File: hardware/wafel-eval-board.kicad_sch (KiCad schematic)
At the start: 50 parts, among them J101 CAN PORT, J102 SW, Q101 AO3422, U101 LM5163DDA

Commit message: reduced BOM
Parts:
- F103: footprint wafel-eval-board:Fuse_SMD-3P_5.4x3.2mm -> wafel-eval-board:Fuse_ITV5432
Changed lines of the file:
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@@
 			)
 		)
-		(property "Footprint" "wafel-eval-board:Fuse_SMD-3P_5.4x3.2mm"
+		(property "Footprint" "wafel-eval-board:Fuse_ITV5432"
 			(at 215.9 134.62 0)
 			(hide yes)

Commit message: increased size two times
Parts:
- JP101: footprint Jumper:SolderJumper-3_P2.0mm_Open_TrianglePad1.0x1.5mm -> Jumper:SolderJumper-3_P1.3mm_Open_Pad1.0x1.5mm
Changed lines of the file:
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@@
 			)
 		)
-		(property "Footprint" "Jumper:SolderJumper-3_P2.0mm_Open_TrianglePad1.0x1.5mm"
+		(property "Footprint" "Jumper:SolderJumper-3_P1.3mm_Open_Pad1.0x1.5mm"
 			(at 242.57 125.73 0)
 			(hide yes)

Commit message: ADD ZONES
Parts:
- added H117: BAT+, MountingHole:MountingHole_3.2mm_M3_Pad, symbol Mechanical:MountingHole_Pad
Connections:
- net CELL10: no longer F102.1, F103.1
- new net: F102.1, F103.1, H117.1
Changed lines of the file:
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@@
 		)
 	)
-	(label "CELL10"
-		(at 204.47 142.24 180)
-		(effects
-			(font
-				(size 1.27 1.27)
-			)
-			(justify right bottom)
-		)
-	)
 	(label "FUSE"
 		(at 139.7 77.47 180)
@@
 					(unit 1)
 				)
+			)
+		)
+	)
+	(symbol
+		(lib_id "Mechanical:MountingHole_Pad")
+		(at 201.93 142.24 90)
+		(mirror x)
+		(unit 1)
+		(body_style 1)
+		(exclude_from_sim no)
+		(in_bom no)
+		(on_board yes)
+		(in_pos_files yes)
+		(dnp no)
+		(property "Reference" "H117"
+			(at 193.04 140.97 90)
+			(show_name no)
+			(do_not_autoplace no)
+			(effects
+				(font
+					(size 1.27 1.27)
+				)
+				(justify right)
+			)
+		)
+		(property "Value" "BAT+"
+			(at 193.04 143.51 90)
+			(show_name no)
+			(do_not_autoplace no)
+			(effects
+				(font
+					(size 1.27 1.27)
+				)
+				(justify right)
+			)
+		)
+		(property "Footprint" "MountingHole:MountingHole_3.2mm_M3_Pad"
+			(at 201.93 142.24 0)
+			(hide yes)
+			(show_name no)
+			(do_not_autoplace no)
+			(effects
+				(font
+					(size 1.27 1.27)
+				)
+			)
+		)
+		(property "Datasheet" ""
+			(at 201.93 142.24 0)
+			(hide yes)
+			(show_name no)
+			(do_not_autoplace no)
+			(effects
+				(font
+					(size 1.27 1.27)
+				)
+			)
+		)
+		(property "Description" "Mounting Hole with connection"
+			(at 201.93 142.24 0)
+			(hide yes)
+			(show_name no)
+			(do_not_autoplace no)
+			(effects
+				(font
+					(size 1.27 1.27)
+				)
+			)
+		)
+		(pin "1"
+		)
+		(instances
+			(project "wafel-eval-board"
+				(path "/3e668e3e-3e16-4665-a807-4735962c41d3"
+					(reference "H117")
+					(unit 1)
+				)

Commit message: Actualize resistors size
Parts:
- added R112: 0, Resistor_SMD:R_0603_1608Metric, symbol Device:R_Small
- D102: footprint LED_THT:LED_D3.0mm -> LED_SMD:LED_0201_0603Metric
- R104, R105: footprint Resistor_SMD:R_0603_1608Metric -> Resistor_SMD:R_2512_6332Metric
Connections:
- net GND: now also R112.1; no longer H106.1, R104.1, R105.1
- new net BAT-: H106.1, R104.1, R105.1, R112.2
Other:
- sheet Frontend ports: added none; removed BAT+
- sheet High-Side N-MOSFET ports: added BAT-; removed none
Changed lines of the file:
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@@
 	(wire
 		(pts
-			(xy 101.6 101.6) (xy 101.6 99.06)
-		)
-		(stroke
-			(width 0)
-			(type default)
-		)
-	)
-	(wire
-		(pts
 			(xy 53.34 149.86) (xy 53.34 140.97)
 		)
@@
 		)
 	)
+	(wire
+		(pts
+			(xy 142.24 97.79) (xy 149.86 97.79)
+		)
+		(stroke
+			(width 0)
+			(type default)
+		)
+	)
 	(bus
 		(pts
@@
 	(wire
 		(pts
-			(xy 96.52 72.39) (xy 106.68 72.39)
-		)
-		(stroke
-			(width 0)
-			(type default)
-		)
-	)
-	(wire
-		(pts
 			(xy 187.96 87.63) (xy 196.85 87.63)
 		)
@@
 	(wire
 		(pts
-			(xy 142.24 97.79) (xy 149.86 97.79)
+			(xy 142.24 92.71) (xy 149.86 92.71)
 		)
 		(stroke
@@
 	(wire
 		(pts
+			(xy 39.37 87.63) (xy 39.37 91.44)
+		)
+		(stroke
+			(width 0)
+			(type default)
+		)
+	)
+	(wire
+		(pts
 			(xy 24.13 128.27) (xy 25.4 128.27)
 		)
@@
 	(wire
 		(pts
-			(xy 39.37 78.74) (xy 39.37 83.82)
+			(xy 39.37 78.74) (xy 39.37 82.55)
 		)
 		(stroke
@@
 		)
 	)
-	(label "BAT+"
-		(at 96.52 72.39 0)
+	(label "BAT-"
+		(at 142.24 97.79 0)
 		(effects
 			(font
@@
 		)
 	)
+	(label "BAT-"
+		(at 101.6 99.06 0)
+		(effects
+			(font
+				(size 1.27 1.27)
+			)
+			(justify left bottom)
+		)
+	)
 	(label "CELL5"
 		(at 57.15 63.5 180)
@@
 		)
 	)
+	(label "BAT-"
+		(at 39.37 81.28 0)
+		(effects
+			(font
+				(size 1.27 1.27)
+			)
+			(justify left bottom)
+		)
+	)
 	(label "CAN.H"
 		(at 210.82 58.42 180)
@@
 	)
 	(label "BAT+"
-		(at 142.24 97.79 0)
+		(at 142.24 92.71 0)
 		(effects
 			(font
@@
 	)
 	(symbol
-		(lib_id "power:GND")
-		(at 101.6 101.6 0)
-		(unit 1)
-		(body_style 1)
-		(exclude_from_sim no)
-		(in_bom yes)
-		(on_board yes)
-		(in_pos_files yes)
-		(dnp no)
-		(fields_autoplaced yes)
-		(property "Reference" "#PWR0105"
-			(at 101.6 107.95 0)
-			(hide yes)
-			(show_name no)
-			(do_not_autoplace no)
-			(effects
-				(font
-					(size 1.27 1.27)
-				)
-			)
-		)
-		(property "Value" "GND"
-			(at 101.6 106.68 0)
-			(show_name no)
-			(do_not_autoplace no)
-			(effects
-				(font
-					(size 1.27 1.27)
-				)
-			)
-		)
-		(property "Footprint" ""
-			(at 101.6 101.6 0)
-			(hide yes)
-			(show_name no)
-			(do_not_autoplace no)
-			(effects
-				(font
-					(size 1.27 1.27)
-				)
-			)
-		)
-		(property "Datasheet" ""
-			(at 101.6 101.6 0)
-			(hide yes)
-			(show_name no)
-			(do_not_autoplace no)
-			(effects
-				(font
-					(size 1.27 1.27)
-				)
-			)
-		)
-		(property "Description" "Power symbol creates a global label with name \"GND\" , ground"
-			(at 101.6 101.6 0)
-			(hide yes)
-			(show_name no)
-			(do_not_autoplace no)
-			(effects
-				(font
-					(size 1.27 1.27)
-				)
-			)
-		)
-		(pin "1"
-		)
-		(instances
-			(project "wafel-eval-board"
-				(path "/3e668e3e-3e16-4665-a807-4735962c41d3"
-					(reference "#PWR0105")
-					(unit 1)
-				)
-			)
-		)
-	)
-	(symbol
 		(lib_id "Device:R_Small")
 		(at 143.51 140.97 0)
@@
 			)
 		)
-		(property "Footprint" "Resistor_SMD:R_0603_1608Metric"
+		(property "Footprint" "Resistor_SMD:R_2512_6332Metric"
 			(at 119.38 104.14 0)
 			(hide yes)
@@
 			)
 		)
-		(property "Footprint" "LED_THT:LED_D3.0mm"
+		(property "Footprint" "LED_SMD:LED_0201_0603Metric"
 			(at 254 125.73 0)
 			(hide yes)
@@
 	(symbol
 		(lib_id "power:GND")
-		(at 39.37 83.82 0)
+		(at 39.37 91.44 0)
 		(mirror y)
 		(unit 1)
@@
 		(fields_autoplaced yes)
 		(property "Reference" "#PWR0101"
-			(at 39.37 90.17 0)
+			(at 39.37 97.79 0)
 			(hide yes)
 			(show_name no)
@@
 		)
 		(property "Value" "GND"
-			(at 39.37 88.9 0)
+			(at 39.37 96.52 0)
 			(show_name no)
 			(do_not_autoplace no)
@@
 		)
 		(property "Footprint" ""
-			(at 39.37 83.82 0)
+			(at 39.37 91.44 0)
 			(hide yes)
 			(show_name no)
@@
 		)
 		(property "Datasheet" ""
-			(at 39.37 83.82 0)
+			(at 39.37 91.44 0)
 			(hide yes)
 			(show_name no)
@@
 		)
 		(property "Description" "Power symbol creates a global label with name \"GND\" , ground"
-			(at 39.37 83.82 0)
+			(at 39.37 91.44 0)
 			(hide yes)
 			(show_name no)
@@
 			)
 		)
-		(property "Footprint" "Resistor_SMD:R_0603_1608Metric"
+		(property "Footprint" "Resistor_SMD:R_2512_6332Metric"
 			(at 119.38 99.06 0)
 			(hide yes)
@@
 	)
 	(symbol
+		(lib_id "Device:R_Small")
+		(at 39.37 85.09 0)
+		(mirror x)
+		(unit 1)
+		(body_style 1)
+		(exclude_from_sim no)
+		(in_bom yes)
+		(on_board yes)
+		(in_pos_files yes)
+		(dnp no)
+		(property "Reference" "R112"
+			(at 40.64 86.36 0)
+			(show_name no)
+			(do_not_autoplace no)
+			(effects
+				(font
+					(size 1.27 1.27)
+				)
+				(justify left)
+			)
+		)
+		(property "Value" "0"
+			(at 40.64 83.82 0)
+			(show_name no)
+			(do_not_autoplace no)
+			(effects
+				(font
+					(size 1.27 1.27)
+				)
+				(justify left)
+			)
+		)
+		(property "Footprint" "Resistor_SMD:R_0603_1608Metric"
+			(at 39.37 85.09 0)
+			(hide yes)
+			(show_name no)
+			(do_not_autoplace no)
+			(effects
+				(font
+					(size 1.27 1.27)
+				)
+			)
+		)
+		(property "Datasheet" ""
+			(at 39.37 85.09 0)
+			(hide yes)
+			(show_name no)
+			(do_not_autoplace no)
+			(effects
+				(font
+					(size 1.27 1.27)
+				)
+			)
+		)
+		(property "Description" "Resistor, small symbol"
+			(at 39.37 85.09 0)
+			(hide yes)
+			(show_name no)
+			(do_not_autoplace no)
+			(effects
+				(font
+					(size 1.27 1.27)
+				)
+			)
+		)
+		(pin "1"
+		)
+		(pin "2"
+		)
+		(instances
+			(project "wafel-eval-board"
+				(path "/3e668e3e-3e16-4665-a807-4735962c41d3"
+					(reference "R112")
+					(unit 1)
+				)
+			)
+		)
+	)
+	(symbol
 		(lib_id "Mechanical:MountingHole_Pad")
 		(at 48.26 50.8 90)
@@
 			)
 		)
-		(pin "BAT+" input
-			(at 106.68 72.39 180)
-			(effects
-				(font
-					(size 1.27 1.27)
-				)
-				(justify left)
-			)
-		)
 		(pin "{FET_CTRL}" output
 			(at 132.08 85.09 0)
@@
 		)
 		(pin "BAT+" input
-			(at 149.86 97.79 180)
+			(at 149.86 92.71 180)
 			(effects
 				(font
@@
 			(effects
 				(font
+					(size 1.27 1.27)
+				)
+				(justify left)
+			)
+		)
+		(pin "BAT-" input
+			(at 149.86 97.79 180)
+			(effects
+				(font

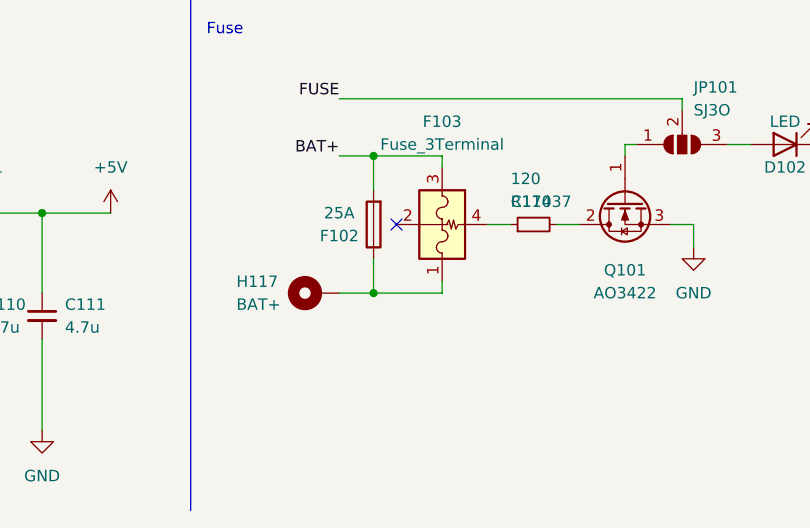
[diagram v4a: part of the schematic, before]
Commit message: Update C301-C306 to 1206 100V capacitors
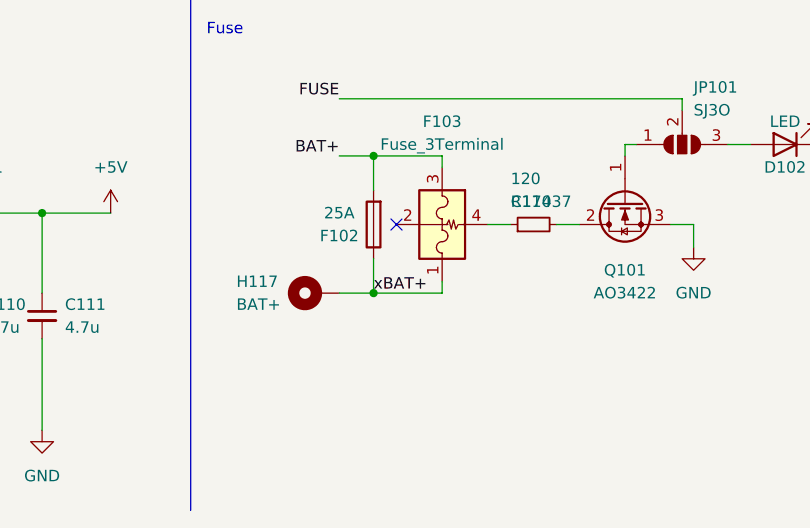
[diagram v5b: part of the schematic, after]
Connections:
- net xBAT+: now reaches F102.1, F103.1, H117.1
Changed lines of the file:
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@@
+		)
+	)
+	(label "xBAT+"
+		(at 208.28 142.24 0)
+		(effects
+			(font
+				(size 1.27 1.27)
+			)
+			(justify left bottom)
 		)
 	)

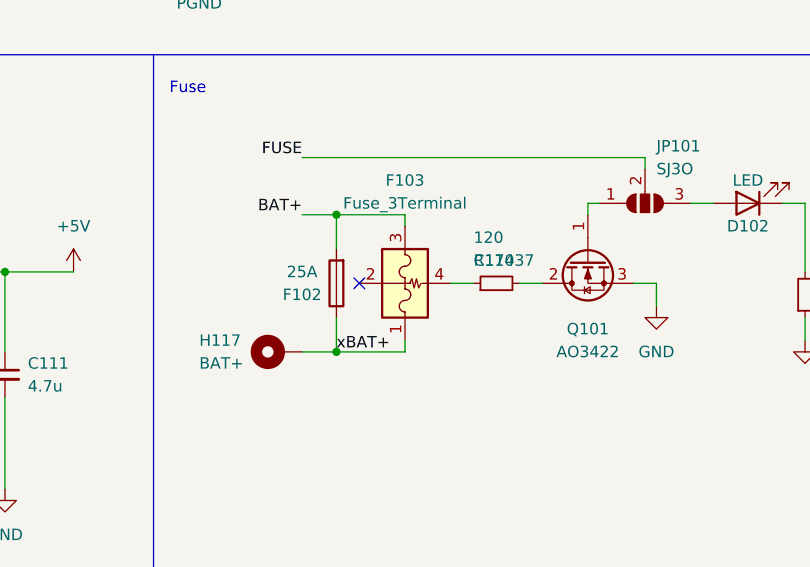
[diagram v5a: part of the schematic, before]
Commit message: Sync PCB layout with updated schematic footprints (Q601/Q701 to SOT-23, C301-C306 to 1206)
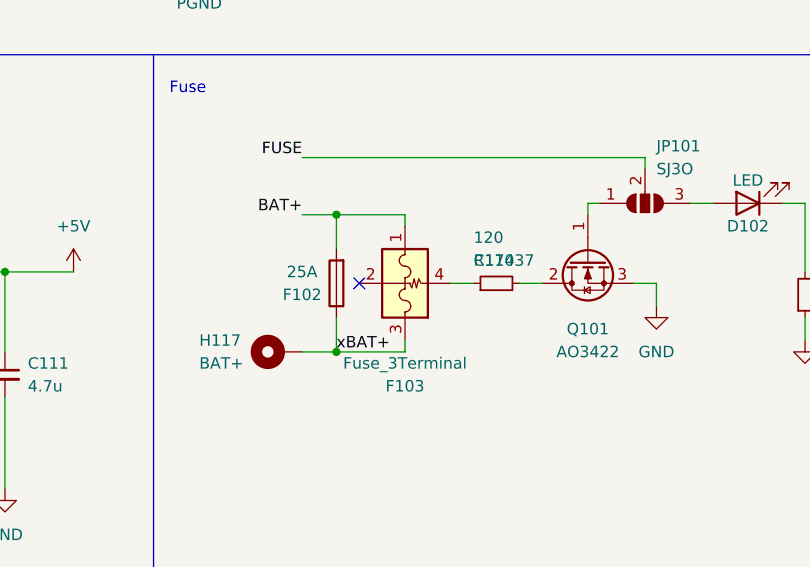
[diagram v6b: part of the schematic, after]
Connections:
- net BAT+: now also F103.1; no longer F103.3
- net xBAT+: now also F103.3; no longer F103.1
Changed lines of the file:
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@@
 		(lib_id "wafel-eval-board:Fuse_3Terminal")
 		(at 215.9 134.62 270)
+		(mirror x)
 		(unit 1)
 		(body_style 1)
@@
 		(dnp no)
 		(property "Reference" "F103"
-			(at 215.9 123.19 90)
+			(at 215.9 146.05 90)
 			(show_name no)
 			(do_not_autoplace no)
@@
 		)
 		(property "Value" "Fuse_3Terminal"
-			(at 215.9 125.73 90)
+			(at 215.9 143.51 90)
 			(show_name no)
 			(do_not_autoplace no)

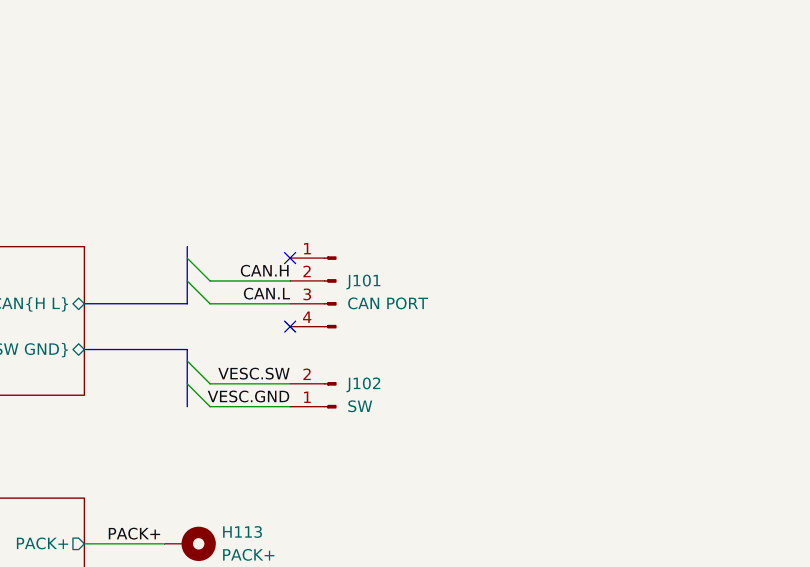
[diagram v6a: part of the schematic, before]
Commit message: added qulon zone
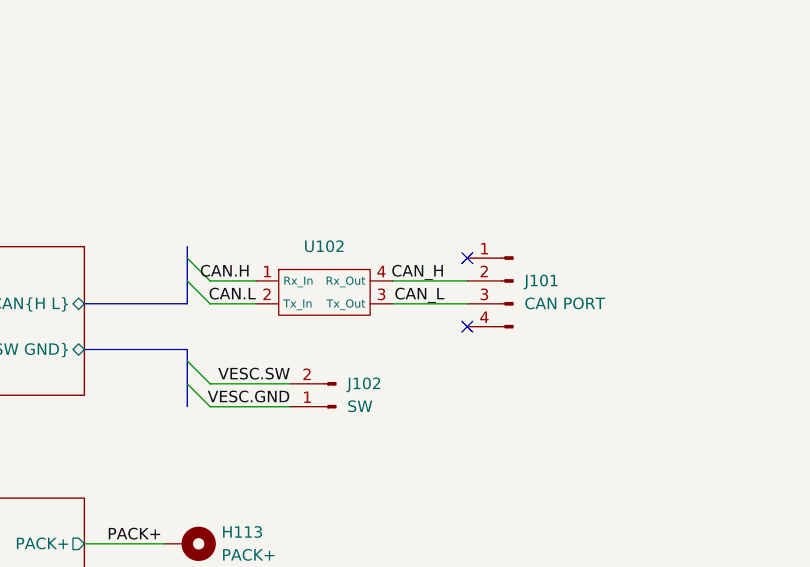
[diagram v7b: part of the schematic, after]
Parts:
- added U102: (no value), wafel-eval-board:poka-yoke_rxtx, symbol wafel-eval-board:poka_yoke_txrx
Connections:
- net CAN.H: now also U102.1 (Rx_In); no longer J101.2 (Pin_2)
- net CAN.L: now also U102.2 (Tx_In); no longer J101.3 (Pin_3)
- new net CAN_H: J101.2 (Pin_2), U102.4 (Rx_Out)
- new net CAN_L: J101.3 (Pin_3), U102.3 (Tx_Out)
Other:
- moved on the sheet: J101
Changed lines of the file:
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@@
 	)
 	(no_connect
-		(at 210.82 63.5)
+		(at 230.505 63.5)
 	)
 	(no_connect
-		(at 210.82 55.88)
+		(at 230.505 55.88)
 	)
 	(no_connect
@@
 	(wire
 		(pts
+			(xy 201.93 58.42) (xy 207.01 58.42)
+		)
+		(stroke
+			(width 0)
+			(type default)
+		)
+	)
+	(wire
+		(pts
 			(xy 116.84 99.06) (xy 115.57 99.06)
 		)
@@
 	(wire
 		(pts
+			(xy 222.25 58.42) (xy 230.505 58.42)
+		)
+		(stroke
+			(width 0)
+			(type default)
+		)
+	)
+	(wire
+		(pts
 			(xy 143.51 133.35) (xy 143.51 138.43)
 		)
@@
 	(wire
 		(pts
-			(xy 201.93 60.96) (xy 210.82 60.96)
-		)
-		(stroke
-			(width 0)
-			(type default)
-		)
-	)
-	(wire
-		(pts
 			(xy 204.47 127) (xy 208.28 127)
 		)
@@
 	(wire
 		(pts
-			(xy 201.93 58.42) (xy 210.82 58.42)
-		)
-		(stroke
-			(width 0)
-			(type default)
-		)
-	)
-	(wire
-		(pts
 			(xy 119.38 133.35) (xy 123.19 133.35)
 		)
@@
 	(wire
 		(pts
+			(xy 201.93 60.96) (xy 207.01 60.96)
+		)
+		(stroke
+			(width 0)
+			(type default)
+		)
+	)
+	(wire
+		(pts
 			(xy 260.35 125.73) (xy 260.35 133.35)
 		)
@@
 	(wire
 		(pts
+			(xy 222.25 60.96) (xy 230.505 60.96)
+		)
+		(stroke
+			(width 0)
+			(type default)
+		)
+	)
+	(wire
+		(pts
 			(xy 71.12 140.97) (xy 71.12 149.86)
 		)
@@
 		)
 	)
+	(label "CAN_L"
+		(at 227.965 60.96 180)
+		(effects
+			(font
+				(size 1.27 1.27)
+			)
+			(justify right bottom)
+		)
+	)
 	(label "VESC.GND"
 		(at 210.82 72.39 180)
@@
 		)
 	)
+	(label "CAN_H"
+		(at 227.965 58.42 180)
+		(effects
+			(font
+				(size 1.27 1.27)
+			)
+			(justify right bottom)
+		)
+	)
 	(label "CELL4"
 		(at 57.15 66.04 180)
@@
 		)
 	)
+	(label "CAN.H"
+		(at 206.375 58.42 180)
+		(effects
+			(font
+				(size 1.27 1.27)
+			)
+			(justify right bottom)
+		)
+	)
 	(label "VESC.SW"
 		(at 210.82 69.85 180)
@@
 	)
 	(label "CAN.L"
-		(at 210.82 60.96 180)
+		(at 207.01 60.96 180)
 		(effects
 			(font
@@
 		)
 	)
-	(label "CAN.H"
-		(at 210.82 58.42 180)
-		(effects
-			(font
-				(size 1.27 1.27)
-			)
-			(justify right bottom)
-		)
-	)
 	(label "CELL10"
 		(at 57.15 50.8 180)
@@
 	)
 	(symbol
+		(lib_id "wafel-eval-board:poka_yoke_txrx")
+		(at 214.63 59.69 0)
+		(unit 1)
+		(body_style 1)
+		(exclude_from_sim no)
+		(in_bom yes)
+		(on_board yes)
+		(in_pos_files yes)
+		(dnp no)
+		(fields_autoplaced yes)
+		(property "Reference" "U102"
+			(at 214.63 54.61 0)
+			(show_name no)
+			(do_not_autoplace no)
+			(effects
+				(font
+					(size 1.27 1.27)
+				)
+			)
+		)
+		(property "Value" ""
+			(at 214.63 58.42 0)
+			(show_name no)
+			(do_not_autoplace no)
+			(effects
+				(font
+					(size 1.27 1.27)
+				)
+			)
+		)
+		(property "Footprint" "wafel-eval-board:poka-yoke_rxtx"
+			(at 215.9 63.5 0)
+			(hide yes)
+			(show_name no)
+			(do_not_autoplace no)
+			(effects
+				(font
+					(size 1.27 1.27)
+				)
+			)
+		)
+		(property "Datasheet" ""
+			(at 214.63 58.42 0)
+			(hide yes)
+			(show_name no)
+			(do_not_autoplace no)
+			(effects
+				(font
+					(size 1.27 1.27)
+				)
+			)
+		)
+		(property "Description" ""
+			(at 214.63 59.69 0)
+			(hide yes)
+			(show_name no)
+			(do_not_autoplace no)
+			(effects
+				(font
+					(size 1.27 1.27)
+				)
+			)
+		)
+		(pin "3"
+		)
+		(pin "1"
+		)
+		(pin "2"
+		)
+		(pin "4"
+		)
+		(instances
+			(project "wafel-eval-board"
+				(path "/3e668e3e-3e16-4665-a807-4735962c41d3"
+					(reference "U102")
+					(unit 1)
+				)
+			)
+		)
+	)
+	(symbol
 		(lib_id "Mechanical:MountingHole_Pad")
 		(at 199.39 97.79 270)
@@
 	(symbol
 		(lib_id "Connector:Conn_01x04_Pin")
-		(at 215.9 58.42 0)
+		(at 235.585 58.42 0)
 		(mirror y)
 		(unit 1)
@@
 		(fields_autoplaced yes)
 		(property "Reference" "J101"
-			(at 217.17 58.4199 0)
+			(at 236.855 58.4199 0)
 			(show_name no)
 			(do_not_autoplace no)
@@
 		)
 		(property "Value" "CAN PORT"
-			(at 217.17 60.9599 0)
+			(at 236.855 60.9599 0)
 			(show_name no)
 			(do_not_autoplace no)
@@
 		)
 		(property "Footprint" "Connector_JST:JST_PH_S4B-PH-K_1x04_P2.00mm_Horizontal"
-			(at 215.9 58.42 0)
+			(at 235.585 58.42 0)
 			(hide yes)
 			(show_name no)
@@
 		)
 		(property "Datasheet" ""
-			(at 215.9 58.42 0)
+			(at 235.585 58.42 0)
 			(hide yes)
 			(show_name no)
@@
 		)
 		(property "Description" "Generic connector, single row, 01x04, script generated"
-			(at 215.9 58.42 0)
+			(at 235.585 58.42 0)
 			(hide yes)
 			(show_name no)
